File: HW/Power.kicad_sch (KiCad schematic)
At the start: 25 parts, among them U2 TS30042-M000QFNR, U4 fork_p5.0mm, U5 fork_p5.0mm, U6 fork_p5.0mm

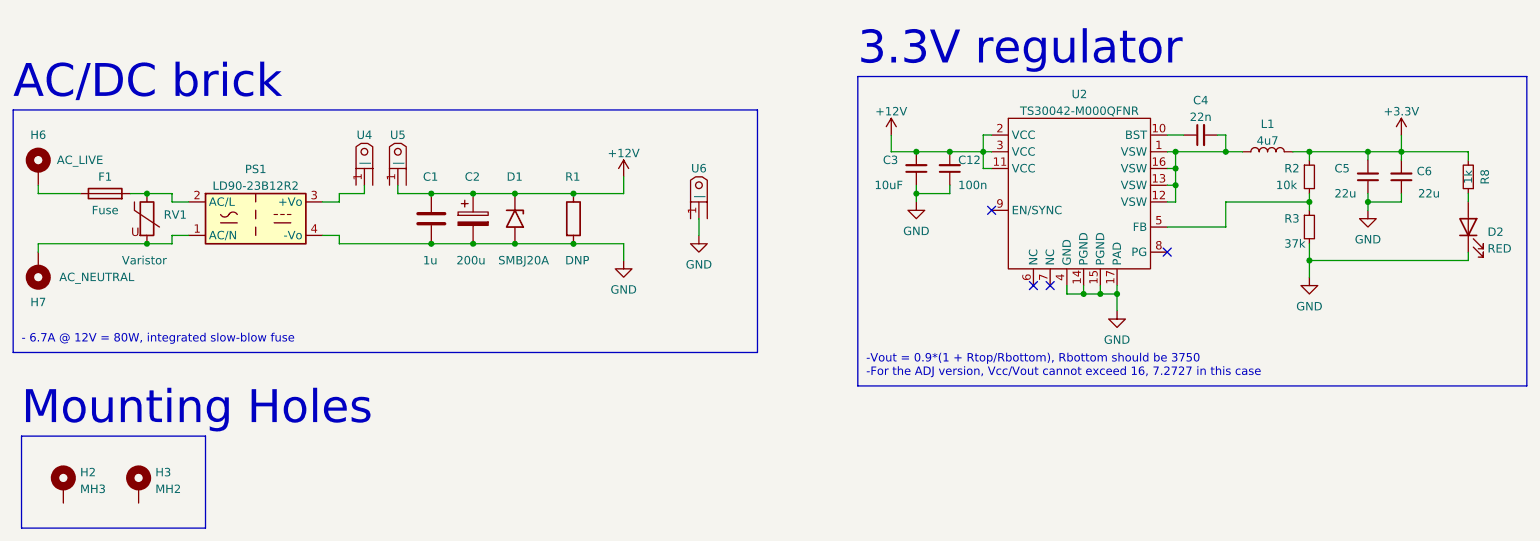
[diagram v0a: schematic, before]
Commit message: Fixed silkscreen, removed one thermistor, fixed component placement
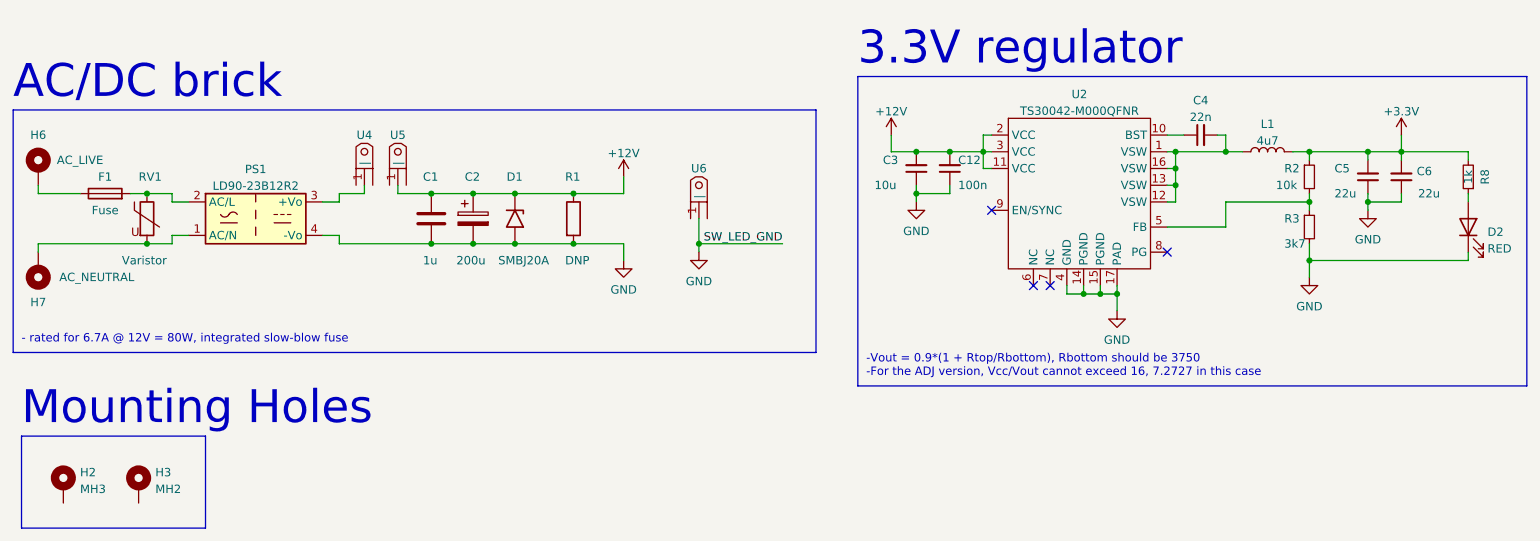
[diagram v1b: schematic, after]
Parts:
- C3: value 10uF -> 10u
- R3: value 37k -> 3k7
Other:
- note added: "- rated for 6.7A @ 12V = 80W, integrated slow-blow fuse"
- note removed: "- 6.7A @ 12V = 80W, integrated slow-blow fuse"
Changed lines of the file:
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@@
   (junction (at 97.79 87.63) (diameter 0) (color 0 0 0 0)
+  )
+  (junction (at 138.43 95.25) (diameter 0) (color 0 0 0 0)
   )
   (junction (at 176.53 81.28) (diameter 0) (color 0 0 0 0)
@@
   (no_connect (at 191.77 101.6))
   (no_connect (at 189.23 101.6))
-  (polyline (pts (xy 147.32 111.76) (xy 147.32 74.93))
+  (polyline (pts (xy 156.21 111.76) (xy 156.21 74.93))
     (stroke (width 0) (type default) (color 0 0 0 0))
   )
@@
     (stroke (width 0) (type default) (color 0 0 0 0))
   )
+  (wire (pts (xy 138.43 95.25) (xy 151.13 95.25))
+    (stroke (width 0) (type default) (color 0 0 0 0))
+  )
   (wire (pts (xy 176.53 86.36) (xy 176.53 87.63))
     (stroke (width 0) (type default) (color 0 0 0 0))
@@
     (stroke (width 0) (type default) (color 0 0 0 0))
   )
+  (wire (pts (xy 138.43 95.25) (xy 138.43 96.52))
+    (stroke (width 0) (type default) (color 0 0 0 0))
+  )
   (wire (pts (xy 231.14 88.9) (xy 231.14 87.63))
     (stroke (width 0) (type default) (color 0 0 0 0))
@@
     (stroke (width 0) (type default) (color 0 0 0 0))
   )
-  (polyline (pts (xy 34.29 111.76) (xy 147.32 111.76))
+  (polyline (pts (xy 34.29 111.76) (xy 156.21 111.76))
     (stroke (width 0) (type default) (color 0 0 0 0))
   )
@@
     (stroke (width 0) (type default) (color 0 0 0 0))
   )
-  (wire (pts (xy 138.43 91.44) (xy 138.43 93.98))
-    (stroke (width 0) (type default) (color 0 0 0 0))
-  )
-  (polyline (pts (xy 34.29 74.93) (xy 147.32 74.93))
+  (wire (pts (xy 138.43 91.44) (xy 138.43 95.25))
+    (stroke (width 0) (type default) (color 0 0 0 0))
+  )
+  (polyline (pts (xy 34.29 74.93) (xy 156.21 74.93))
     (stroke (width 0) (type default) (color 0 0 0 0))
   )
@@
     (effects (font (size 5 5)) (justify left bottom))
   )
-  (text "- 6.7A @ 12V = 80W, integrated slow-blow fuse" (at 35.56 110.49 0)
+  (text "- rated for 6.7A @ 12V = 80W, integrated slow-blow fuse"
+    (at 35.56 110.49 0)
     (effects (font (size 1.27 1.27)) (justify left bottom))
   )
@@
     (effects (font (size 5 5)) (justify left bottom))
   )
+  (label "SW_LED_GND" (at 151.13 95.25 180)
+    (effects (font (size 1.27 1.27)) (justify right bottom))
+  )
   (symbol (lib_id "Device:C") (at 97.79 91.44 0) (unit 1)
     (in_bom yes) (on_board yes)
@@
   (symbol (lib_id "Device:Varistor") (at 54.61 91.44 0) (unit 1)
     (in_bom yes) (on_board yes)
-    (property "Reference" "RV1" (id 0) (at 57.15 90.8585 0)
+    (property "Reference" "RV1" (id 0) (at 53.34 85.09 0)
       (effects (font (size 1.27 1.27)) (justify left))
     )
@@
       (effects (font (size 1.27 1.27)) (justify right))
     )
-    (property "Value" "10uF" (id 1) (at 165.1 86.36 0)
+    (property "Value" "10u" (id 1) (at 165.1 86.36 0)
       (effects (font (size 1.27 1.27)) (justify right))
     )
@@
     (pin "2")
   )
-  (symbol (lib_id "power:GND") (at 138.43 93.98 0) (unit 1)
-    (in_bom yes) (on_board yes) (fields_autoplaced)
-    (property "Reference" "#PWR0123" (id 0) (at 138.43 100.33 0)
-      (effects (font (size 1.27 1.27)) hide)
-    )
-    (property "Value" "GND" (id 1) (at 138.43 98.4234 0))
-    (property "Footprint" "" (id 2) (at 138.43 93.98 0)
-      (effects (font (size 1.27 1.27)) hide)
-    )
-    (property "Datasheet" "" (id 3) (at 138.43 93.98 0)
+  (symbol (lib_id "power:GND") (at 138.43 96.52 0) (unit 1)
+    (in_bom yes) (on_board yes) (fields_autoplaced)
+    (property "Reference" "#PWR0123" (id 0) (at 138.43 102.87 0)
+      (effects (font (size 1.27 1.27)) hide)
+    )
+    (property "Value" "GND" (id 1) (at 138.43 100.9634 0))
+    (property "Footprint" "" (id 2) (at 138.43 96.52 0)
+      (effects (font (size 1.27 1.27)) hide)
+    )
+    (property "Datasheet" "" (id 3) (at 138.43 96.52 0)
       (effects (font (size 1.27 1.27)) hide)
     )
@@
       (effects (font (size 1.27 1.27)) (justify left))
     )
-    (property "Value" "37k" (id 1) (at 227.33 95.25 0)
-      (effects (font (size 1.27 1.27)) (justify left))
-    )
+    (property "Value" "3k7" (id 1) (at 227.33 95.25 0)
+      (effects (font (size 1.27 1.27)) (justify left))
+    )
